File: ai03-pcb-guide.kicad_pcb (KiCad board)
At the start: 2 copper layers, 77.8 x 38.1 mm, 24 parts, among them SW1 SW_Push, U1 ATmega32U4-A, Y1 16MHz

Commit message: probably routed now
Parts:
- D1, D2, D3, D4: moved to B.Cu
- moved D1 19.2 mm to (171.6, 104.8)
- moved D3 19.2 mm to (171.6, 123.8)
- moved D2 18.9 mm to (152.5, 104.8)
- moved D4 18.9 mm to (152.5, 123.8)
- moved C5 7.15 mm to (113.5, 125.7), turned to -90 degrees
- moved C2 1.83 mm to (114.3, 110.3), turned to 90 degrees
- moved SW1 1.77 mm to (102.4, 129.9)
- moved R2 1.59 mm to (105.6, 107.0), turned to -90 degrees
- moved R3 1.59 mm to (102.4, 107.0), turned to -90 degrees
- moved C1 1.31 mm to (112.5, 119.1)
- moved R4 0.97 mm to (110.1, 110.5), turned to -90 degrees
- moved F1 0.79 mm to (98.4, 111.3), turned to -90 degrees
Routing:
- net GND: track 0.00 -> 156.5 mm
- net +5V: track 0.00 -> 111.7 mm, vias 0 -> 6
- net Net-(U1-~{RESET}): track 0.00 -> 33.2 mm, vias 0 -> 3
- net Net-(U1-D-): track 0.00 -> 26.2 mm
- net Net-(U1-D+): track 0.00 -> 25.6 mm
- net ROW1: track 0.00 -> 21.7 mm
- net ROW0: track 0.00 -> 20.9 mm
- net COL1: track 0.00 -> 19.0 mm
- net COL0: track 0.00 -> 19.0 mm
- net Net-(U1-XTAL2): track 0.00 -> 12.7 mm
- net Net-(U1-XTAL1): track 0.00 -> 10.4 mm
- net VCC: track 0.00 -> 10.3 mm
- net Net-(D3-A): track 0.00 -> 7.59 mm
- net Net-(D4-A): track 0.00 -> 7.31 mm
- net Net-(D1-A): track 0.00 -> 7.07 mm
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
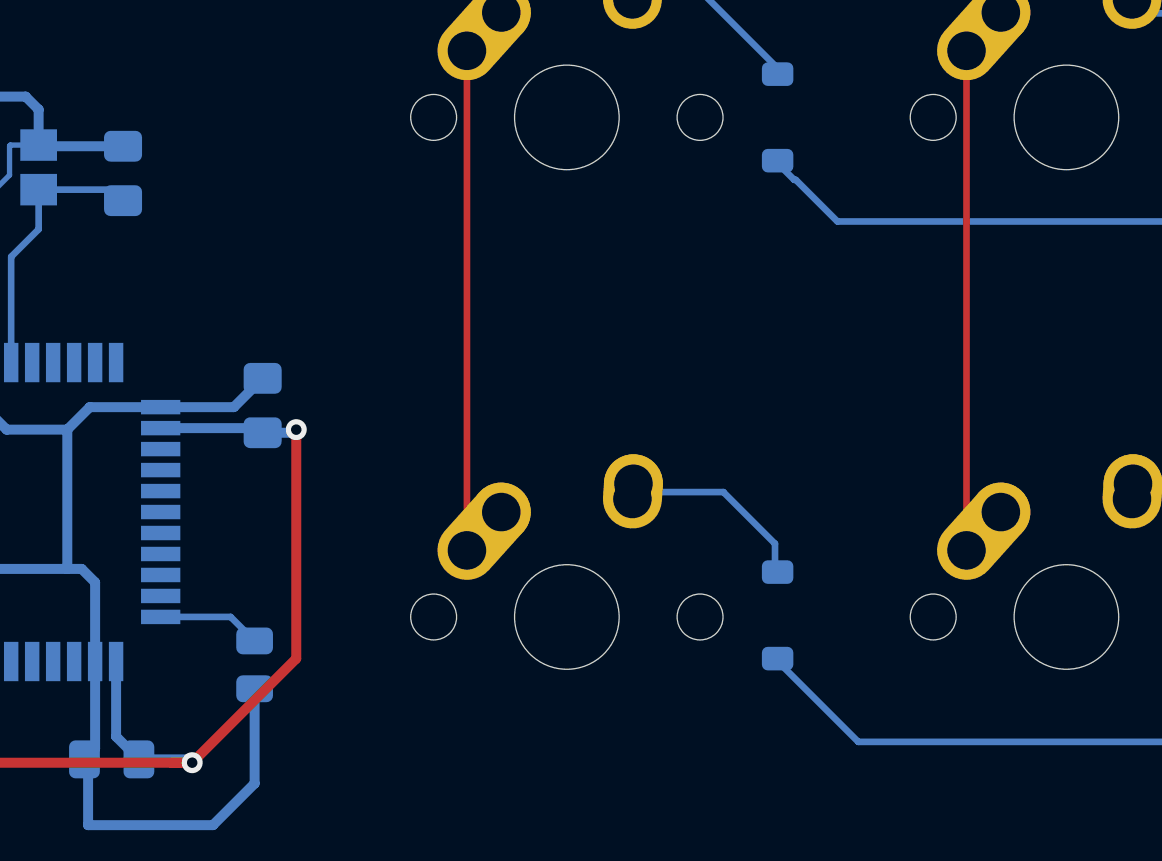
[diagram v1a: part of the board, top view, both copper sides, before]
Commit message: added matrix to mcu pins
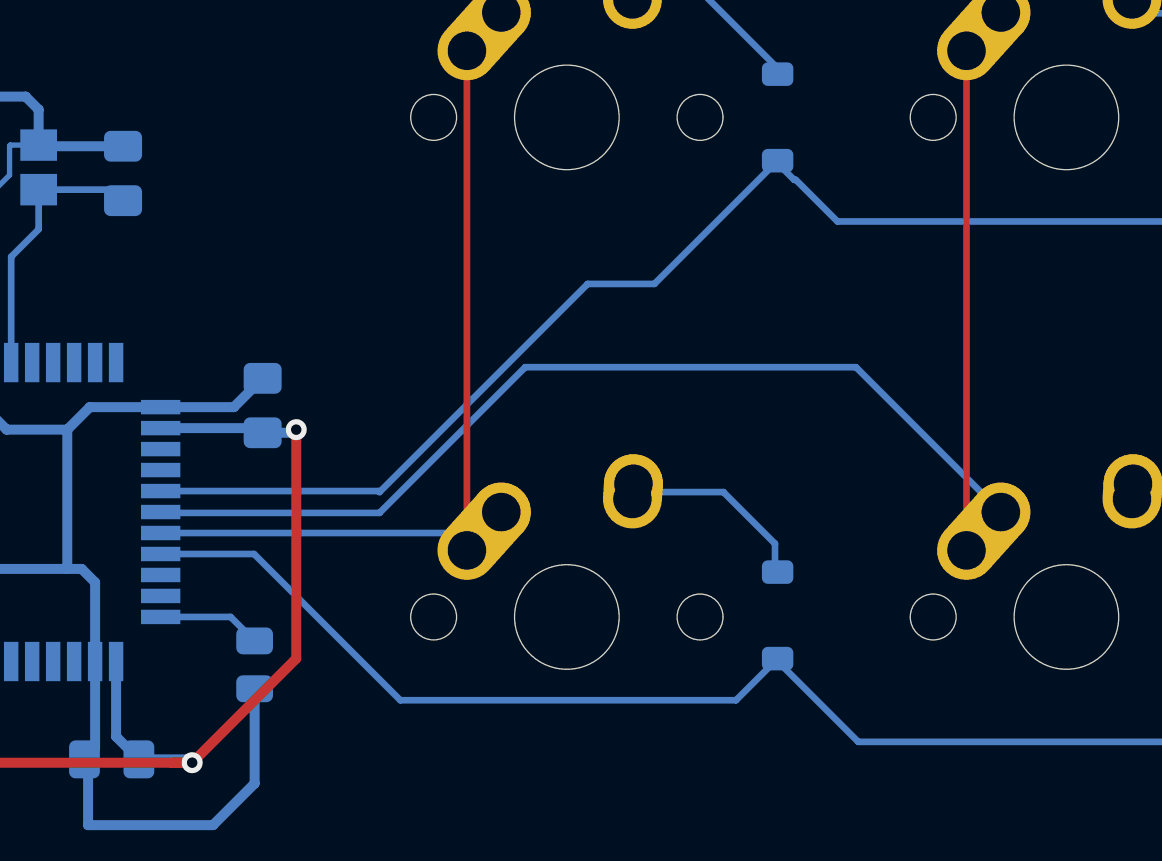
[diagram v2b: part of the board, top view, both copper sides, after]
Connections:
- U1 pad 27: unconnected-(U1-PD7-Pad27) -> ROW0
- U1 pad 28: unconnected-(U1-PB4-Pad28) -> COL1
- U1 pad 29: unconnected-(U1-PB5-Pad29) -> COL0
- U1 pad 30: unconnected-(U1-PB6-Pad30) -> ROW1
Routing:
- net COL1: track 19.0 -> 55.7 mm
- net ROW0: track 20.9 -> 49.7 mm
- net ROW1: track 21.7 -> 48.1 mm
- net COL0: track 19.0 -> 31.0 mm

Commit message: generated gerber files
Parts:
- moved D1 19.2 mm to (152.4, 103.1)
- moved D3 19.2 mm to (152.4, 123.0)
- moved D2 19.0 mm to (171.4, 103.2)
- moved D4 18.9 mm to (171.4, 123.8)
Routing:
- net ROW0: track 49.7 -> 53.6 mm
- net ROW1: track 48.1 -> 49.2 mm
- net Net-(D3-A): track 7.59 -> 6.60 mm
- net Net-(D1-A): track 7.07 -> 6.13 mm
- net +5V: track 111.7 -> 110.9 mm, vias 6 -> 5
- net Net-(D2-A): track 6.64 -> 5.96 mm
- net GND: track 156.5 -> 155.9 mm
- net Net-(U1-~{RESET}): track 33.2 -> 32.9 mm, vias 3 -> 2
- added copper zone on B.Cu, net GND
